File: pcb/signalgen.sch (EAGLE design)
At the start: 30 parts, among them U1 MSP430G2553, U2 TL974IN, U3 TLV4112CP, U4 LD1117-PTH, X1 MST2V, X2 MKDSN1,5/2-5,08

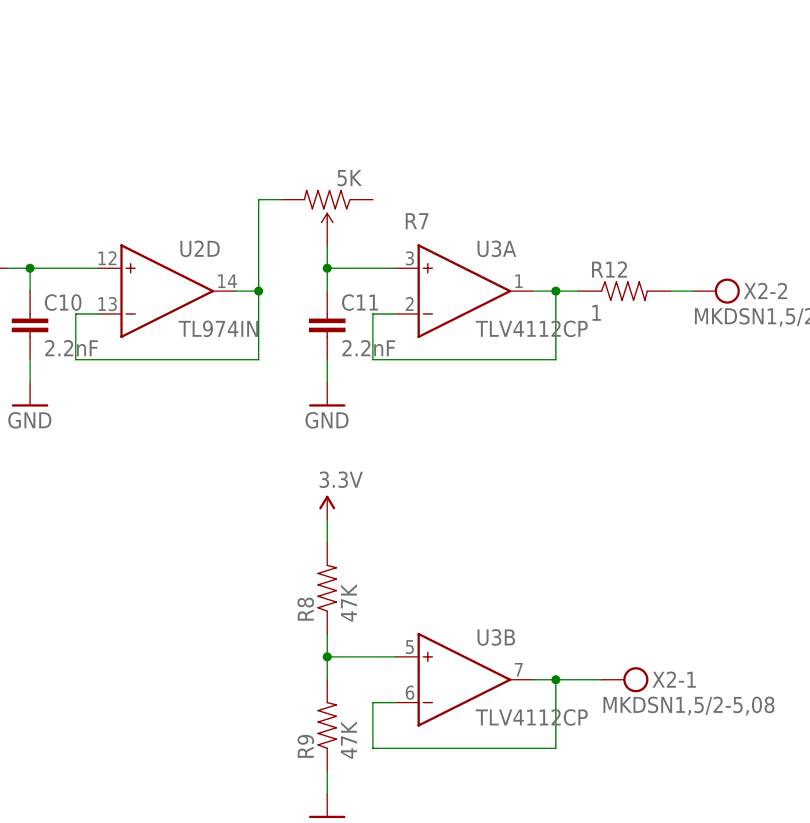
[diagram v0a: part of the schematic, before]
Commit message: Implemented system linearization
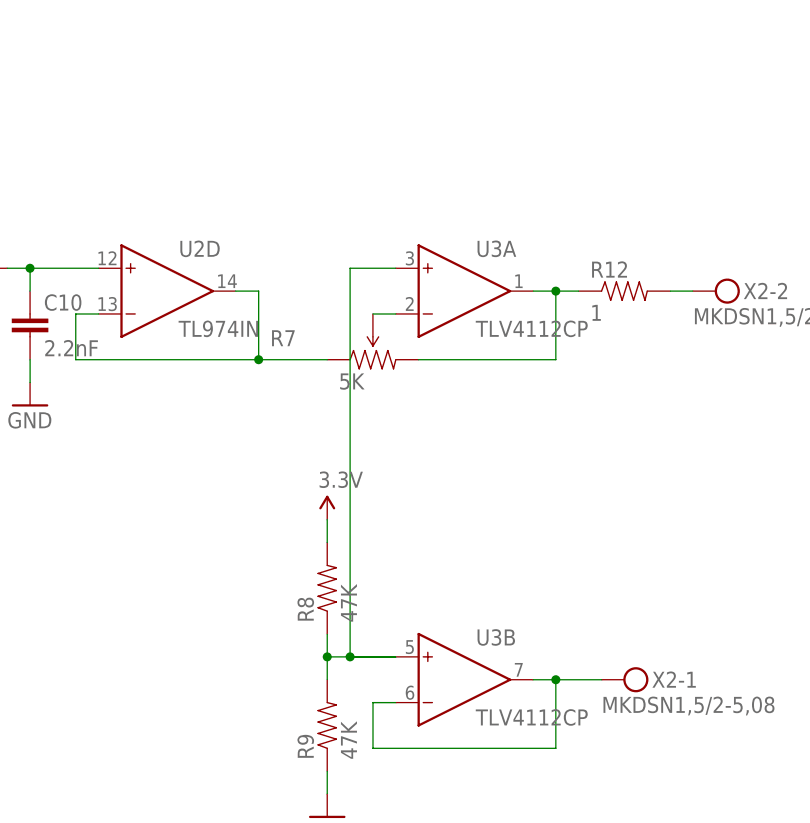
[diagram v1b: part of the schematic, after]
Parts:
- removed C11: 2.2nF, SparkFun-Capacitors:CAPPTH
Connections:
- net GND: no longer C11.2
- net N$14: now also R7.CCW; no longer R7.CW
- net N$15: now also U3A.IN+
- net N$16: now also R7.CW; no longer U3A.IN-
- net N$18: now also U3A.IN-; no longer C11.1, U3A.IN+
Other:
- moved on the sheet: R7
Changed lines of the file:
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@@
 <part name="R6" library="SparkFun-Resistors" deviceset="1KOHM-1/4W-1%(PTH)" device="" value="1K"/>
 <part name="R7" library="SparkFun-Electromechanical" deviceset="TRIMPOT" device="PTH" value="5K"/>
-<part name="C11" library="SparkFun-Capacitors" deviceset="CAP" device="PTH" value="2.2nF"/>
-<part name="GND14" library="SparkFun-Aesthetics" deviceset="GND" device=""/>
 <part name="R8" library="SparkFun-Resistors" deviceset="1KOHM-1/4W-1%(PTH)" device="" value="47K"/>
 <part name="R9" library="SparkFun-Resistors" deviceset="1KOHM-1/4W-1%(PTH)" device="" value="47K"/>
@@
 <instance part="SUPPLY5" gate="G$1" x="261.62" y="35.56"/>
 <instance part="R6" gate="G$1" x="220.98" y="63.5"/>
-<instance part="R7" gate="R?" x="261.62" y="71.12" rot="R180"/>
-<instance part="C11" gate="G$1" x="261.62" y="55.88"/>
-<instance part="GND14" gate="1" x="261.62" y="48.26"/>
+<instance part="R7" gate="R?" x="266.7" y="53.34"/>
 <instance part="R8" gate="G$1" x="261.62" y="27.94" rot="R90"/>
 <instance part="R9" gate="G$1" x="261.62" y="12.7" rot="R90"/>
@@
 <pinref part="R9" gate="G$1" pin="1"/>
 </segment>
-<segment>
-<pinref part="C11" gate="G$1" pin="2"/>
-<pinref part="GND14" gate="1" pin="GND"/>
-<wire x1="261.62" y1="50.8" x2="261.62" y2="53.34" width="0.1524" layer="91"/>
-</segment>
 </net>
 <net name="N$1" class="0">
@@
 <net name="N$16" class="0">
 <segment>
-<pinref part="U3" gate="A" pin="IN-"/>
-<wire x1="269.24" y1="58.42" x2="266.7" y2="58.42" width="0.1524" layer="91"/>
-<wire x1="266.7" y1="58.42" x2="266.7" y2="53.34" width="0.1524" layer="91"/>
-<wire x1="266.7" y1="53.34" x2="287.02" y2="53.34" width="0.1524" layer="91"/>
+<pinref part="U3" gate="A" pin="OUT"/>
+<pinref part="R12" gate="G$1" pin="1"/>
+<wire x1="284.48" y1="60.96" x2="287.02" y2="60.96" width="0.1524" layer="91"/>
+<pinref part="R7" gate="R?" pin="CW"/>
+<wire x1="287.02" y1="60.96" x2="289.56" y2="60.96" width="0.1524" layer="91"/>
+<wire x1="271.78" y1="53.34" x2="287.02" y2="53.34" width="0.1524" layer="91"/>
 <wire x1="287.02" y1="53.34" x2="287.02" y2="60.96" width="0.1524" layer="91"/>
-<pinref part="U3" gate="A" pin="OUT"/>
-<wire x1="287.02" y1="60.96" x2="284.48" y2="60.96" width="0.1524" layer="91"/>
-<pinref part="R12" gate="G$1" pin="1"/>
-<wire x1="287.02" y1="60.96" x2="289.56" y2="60.96" width="0.1524" layer="91"/>
 <junction x="287.02" y="60.96"/>
 </segment>
@@
 <pinref part="U2" gate="D" pin="OUT"/>
 <wire x1="254" y1="60.96" x2="251.46" y2="60.96" width="0.1524" layer="91"/>
-<pinref part="R7" gate="R?" pin="CW"/>
-<wire x1="256.54" y1="71.12" x2="254" y2="71.12" width="0.1524" layer="91"/>
-<wire x1="254" y1="71.12" x2="254" y2="60.96" width="0.1524" layer="91"/>
-<junction x="254" y="60.96"/>
+<pinref part="R7" gate="R?" pin="CCW"/>
+<wire x1="261.62" y1="53.34" x2="254" y2="53.34" width="0.1524" layer="91"/>
+<junction x="254" y="53.34"/>
 </segment>
 </net>
 <net name="N$15" class="0">
 <segment>
-<pinref part="U3" gate="B" pin="IN+"/>
-<wire x1="269.24" y1="20.32" x2="261.62" y2="20.32" width="0.1524" layer="91"/>
 <wire x1="261.62" y1="17.78" x2="261.62" y2="20.32" width="0.1524" layer="91"/>
-<junction x="261.62" y="20.32"/>
-<wire x1="261.62" y1="20.32" x2="261.62" y2="22.86" width="0.1524" layer="91"/>
 <pinref part="R8" gate="G$1" pin="1"/>
 <pinref part="R9" gate="G$1" pin="2"/>
-</segment>
-</net>
-<net name="N$18" class="0">
-<segment>
-<pinref part="R7" gate="R?" pin="WIPER"/>
-<pinref part="C11" gate="G$1" pin="1"/>
-<wire x1="261.62" y1="66.04" x2="261.62" y2="63.5" width="0.1524" layer="91"/>
-<wire x1="261.62" y1="60.96" x2="261.62" y2="63.5" width="0.1524" layer="91"/>
+<pinref part="U3" gate="B" pin="IN+"/>
+<wire x1="261.62" y1="20.32" x2="261.62" y2="22.86" width="0.1524" layer="91"/>
+<wire x1="261.62" y1="20.32" x2="264.16" y2="20.32" width="0.1524" layer="91"/>
+<wire x1="264.16" y1="20.32" x2="269.24" y2="20.32" width="0.1524" layer="91"/>
+<wire x1="269.24" y1="20.32" x2="264.16" y2="20.32" width="0.1524" layer="91"/>
+<wire x1="264.16" y1="20.32" x2="264.16" y2="63.5" width="0.1524" layer="91"/>
 <pinref part="U3" gate="A" pin="IN+"/>
-<wire x1="261.62" y1="63.5" x2="269.24" y2="63.5" width="0.1524" layer="91"/>
-<junction x="261.62" y="63.5"/>
+<wire x1="264.16" y1="63.5" x2="269.24" y2="63.5" width="0.1524" layer="91"/>
+<junction x="264.16" y="20.32"/>
+<junction x="261.62" y="20.32"/>
 </segment>
 </net>
@@
 </segment>
 </net>
+<net name="N$18" class="0">
+<segment>
+<pinref part="U3" gate="A" pin="IN-"/>
+<pinref part="R7" gate="R?" pin="WIPER"/>
+<wire x1="269.24" y1="58.42" x2="266.7" y2="58.42" width="0.1524" layer="91"/>
+</segment>
+</net>
